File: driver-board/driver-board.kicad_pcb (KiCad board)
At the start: 2 copper layers, 22 parts, among them J1 MCP4725, J2 Conn_Coaxial, SW1 RST, U1 Pico, U2 MIC5317, U3 TSV358, U4 TSV358, U5 TCBT-2R5G

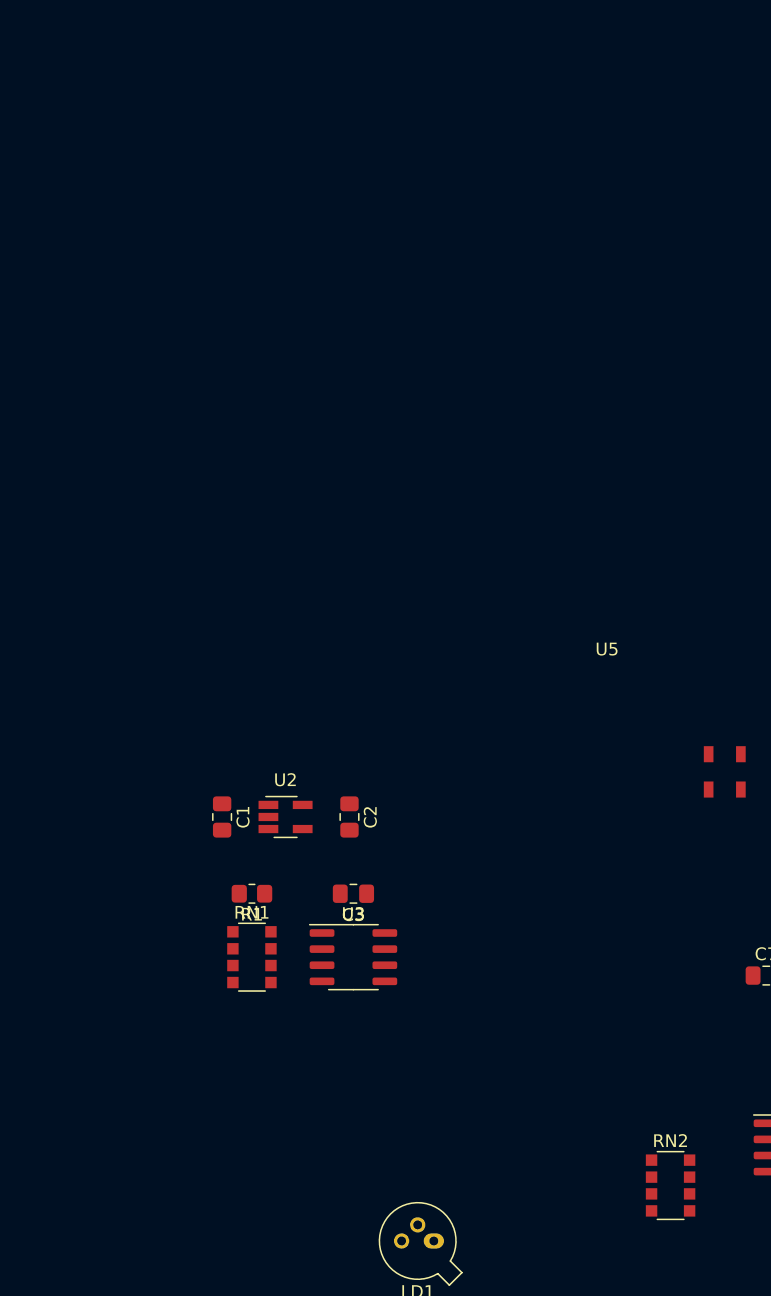
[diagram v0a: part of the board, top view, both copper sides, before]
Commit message: fix pot footprint
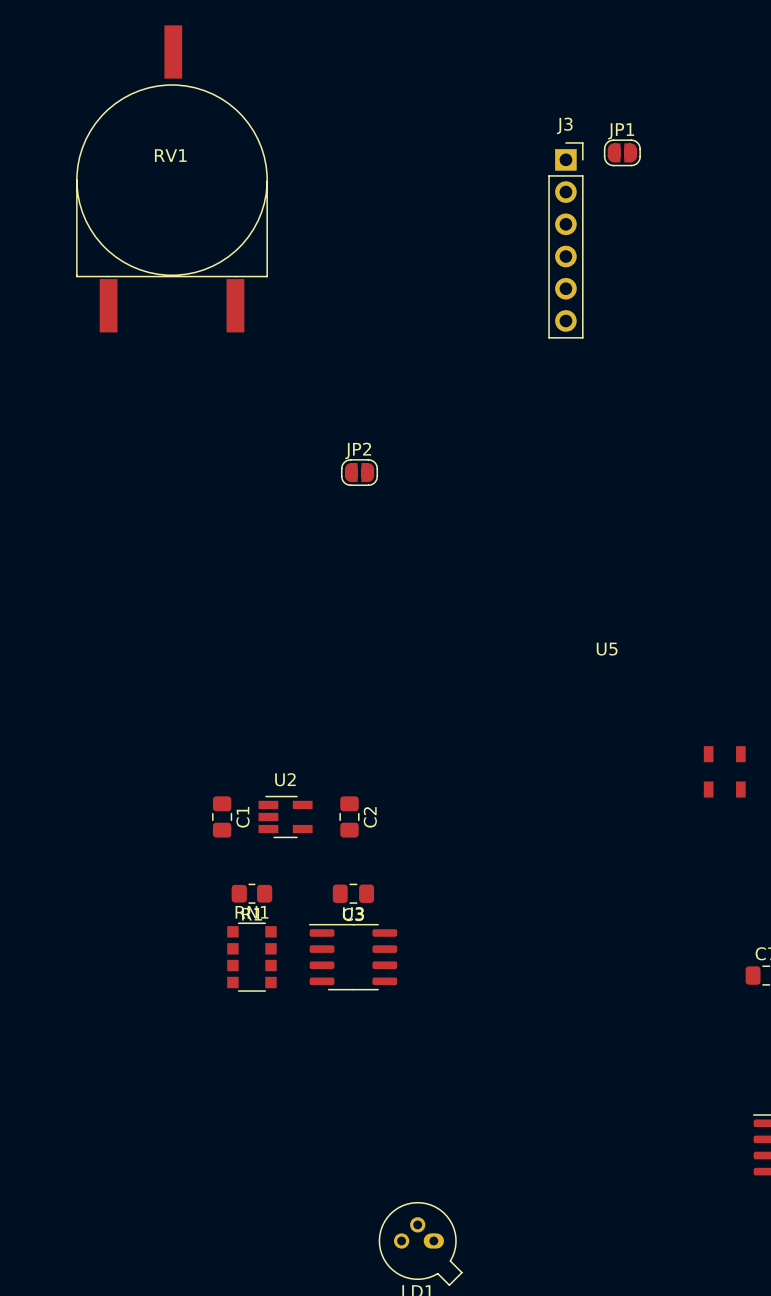
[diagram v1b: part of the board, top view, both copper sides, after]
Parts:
- removed RN2: R_Pack04_SIP_Split, Resistor_SMD:R_Array_Convex_4x1206
- added J3: MCP4725, Connector_PinSocket_2.54mm:PinSocket_1x06_P2.54mm_Vertical, F.Cu at (148.8, 59.1)
- added JP1: SolderJumper_2_Open, Jumper:SolderJumper-2_P1.3mm_Open_RoundedPad1.0x1.5mm, F.Cu at (153.2, 58.6)
- added JP2: SolderJumper_2_Open, Jumper:SolderJumper-2_P1.3mm_Open_RoundedPad1.0x1.5mm, F.Cu at (132.5, 83.8)
- added RV1: R_Potentiometer, lib:PT15-RV15, F.Cu at (117.7, 60.8)
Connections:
- net DAC_OUT renamed DAC_OUT_I_SRC
- U4 pad 5: Net-(U4-Pad1) -> Net-(U4-Pad5)

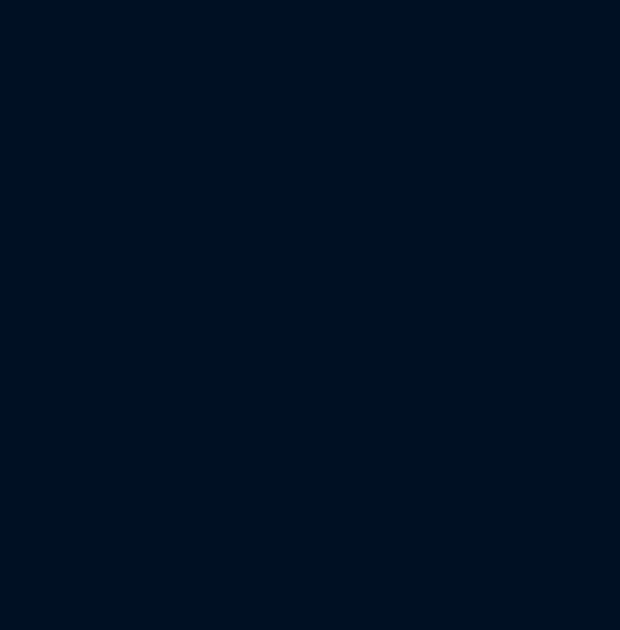
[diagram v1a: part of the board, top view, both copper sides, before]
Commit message: more test points and design rules
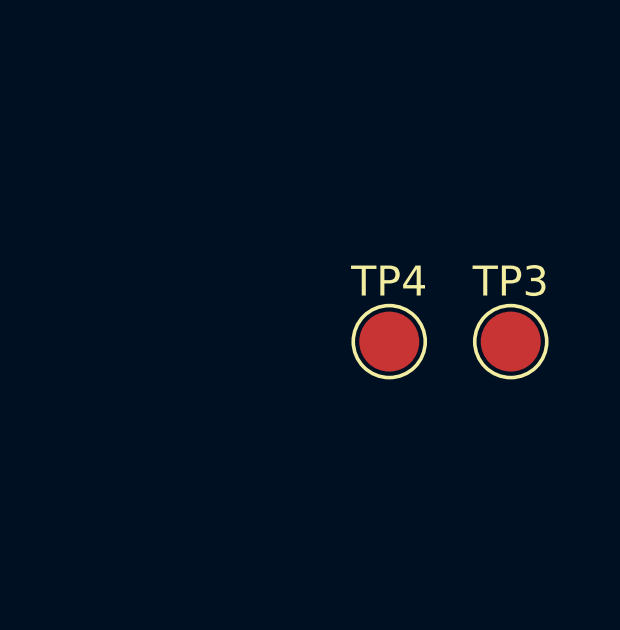
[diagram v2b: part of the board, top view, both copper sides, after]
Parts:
- added TP3: TestPoint, TestPoint:TestPoint_Pad_D2.0mm, F.Cu at (191.7, 71.3)
- added TP4: TestPoint, TestPoint:TestPoint_Pad_D2.0mm, F.Cu at (187.7, 71.3)
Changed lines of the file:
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@@
     (0 "F.Cu" signal)
     (31 "B.Cu" signal)
-    (32 "B.Adhes" user "B.Adhesive")
-    (33 "F.Adhes" user "F.Adhesive")
-    (34 "B.Paste" user)
-    (35 "F.Paste" user)
     (36 "B.SilkS" user "B.Silkscreen")
     (37 "F.SilkS" user "F.Silkscreen")
@@
     (40 "Dwgs.User" user "User.Drawings")
     (41 "Cmts.User" user "User.Comments")
-    (42 "Eco1.User" user "User.Eco1")
-    (43 "Eco2.User" user "User.Eco2")
     (44 "Edge.Cuts" user)
     (45 "Margin" user)
@@
     (48 "B.Fab" user)
     (49 "F.Fab" user)
-    (50 "User.1" user)
-    (51 "User.2" user)
-    (52 "User.3" user)
-    (53 "User.4" user)
-    (54 "User.5" user)
-    (55 "User.6" user)
-    (56 "User.7" user)
-    (57 "User.8" user)
-    (58 "User.9" user)
   )
   (setup
+    (stackup
+      (layer "F.SilkS" (type "Top Silk Screen"))
+      (layer "F.Mask" (type "Top Solder Mask") (thickness 0.01))
+      (layer "F.Cu" (type "copper") (thickness 0.035))
+      (layer "dielectric 1" (type "core") (thickness 1.51) (material "FR4") (epsilon_r 4.5) (loss_tangent 0.02))
+      (layer "B.Cu" (type "copper") (thickness 0.035))
+      (layer "B.Mask" (type "Bottom Solder Mask") (thickness 0.01))
+      (layer "B.SilkS" (type "Bottom Silk Screen"))
+      (copper_finish "None")
+      (dielectric_constraints no)
+    )
     (pad_to_mask_clearance 0)
     (pcbplotparams
@@
   (net 43 "unconnected-(U1-Pad42)")
   (net 44 "unconnected-(U1-Pad43)")
-  (net 45 "Net-(U4-Pad1)")
+  (net 45 "Net-(JP1-Pad1)")
   (net 46 "unconnected-(U5-Pad2)")
   (net 47 "DAC_OUT_TIA")
-  (net 48 "Net-(U4-Pad5)")
+  (net 48 "Net-(JP1-Pad2)")
   (net 49 "Net-(RN1-Pad3)")
   (net 50 "Net-(RN1-Pad5)")
-  (net 51 "Net-(U4-Pad3)")
+  (net 51 "Net-(RV1-Pad2)")
   (footprint "Capacitor_SMD:C_0805_2012Metric_Pad1.18x1.45mm_HandSolder" (layer "F.Cu")
     (at 174 128)
@@
       (net 36 "A3V3") (pinfunction "1") (pintype "passive"))
     (pad "2" smd rect (at 0.1 -10.1) (size 1.4 4.2) (layers "F.Cu" "F.Paste" "F.Mask")
-      (net 51 "Net-(U4-Pad3)") (pinfunction "2") (pintype "passive"))
+      (net 51 "Net-(RV1-Pad2)") (pinfunction "2") (pintype "passive"))
     (pad "3" smd rect (at 5 9.9) (size 1.4 4.2) (layers "F.Cu" "F.Paste" "F.Mask")
       (net 2 "GND") (pinfunction "3") (pintype "passive"))
+  )
+  (footprint "TestPoint:TestPoint_Pad_D2.0mm" (layer "F.Cu")
+    (at 187.65 71.3)
+    (descr "SMD pad as test Point, diameter 2.0mm")
+    (tags "test point SMD pad")
+    (property "Sheetfile" "driver-board.kicad_sch")
+    (property "Sheetname" "")
+    (attr exclude_from_pos_files)
+    (fp_text reference "TP4" (at 0 -1.998) (layer "F.SilkS")
+      (effects (font (size 1 1) (thickness 0.15)))
+    )
+    (fp_text value "TestPoint" (at 0 2.05) (layer "F.Fab")
+      (effects (font (size 1 1) (thickness 0.15)))
+    )
+    (fp_text user "${REFERENCE}" (at 0 -2) (layer "F.Fab")
+      (effects (font (size 1 1) (thickness 0.15)))
+    )
+    (fp_circle (center 0 0) (end 0 1.2) (layer "F.SilkS") (width 0.12) (fill none))
+    (fp_circle (center 0 0) (end 1.5 0) (layer "F.CrtYd") (width 0.05) (fill none))
+    (pad "1" smd circle locked (at 0 0) (size 2 2) (layers "F.Cu" "F.Mask")
+      (net 39 "TIA_OUT") (pinfunction "1") (pintype "passive"))
   )
   (footprint "Connector_PinSocket_2.54mm:PinSocket_1x06_P2.54mm_Vertical" (layer "F.Cu")
@@
     (fp_line (start -1.65 -1.25) (end 1.65 -1.25) (layer "F.CrtYd") (width 0.05))
     (pad "1" smd custom locked (at -0.65 0) (size 1 0.5) (layers "F.Cu" "F.Mask")
-      (net 45 "Net-(U4-Pad1)") (pinfunction "A") (pintype "passive") (zone_connect 2)
+      (net 45 "Net-(JP1-Pad1)") (pinfunction "A") (pintype "passive") (zone_connect 2)
       (options (clearance outline) (anchor rect))
       (primitives
@@
       ))
     (pad "2" smd custom locked (at 0.65 0) (size 1 0.5) (layers "F.Cu" "F.Mask")
-      (net 48 "Net-(U4-Pad5)") (pinfunction "B") (pintype "passive") (zone_connect 2)
+      (net 48 "Net-(JP1-Pad2)") (pinfunction "B") (pintype "passive") (zone_connect 2)
       (options (clearance outline) (anchor rect))
       (primitives
@@
     (fp_line (start 1.95 2.45) (end -1.95 2.45) (layer "F.Fab") (width 0.1))
     (pad "1" smd roundrect (at -2.475 -1.905) (size 1.95 0.6) (layers "F.Cu" "F.Paste" "F.Mask") (roundrect_rratio 0.25)
-      (net 45 "Net-(U4-Pad1)") (pintype "output"))
+      (net 45 "Net-(JP1-Pad1)") (pintype "output"))
     (pad "2" smd roundrect (at -2.475 -0.635) (size 1.95 0.6) (layers "F.Cu" "F.Paste" "F.Mask") (roundrect_rratio 0.25)
-      (net 45 "Net-(U4-Pad1)") (pinfunction "-") (pintype "input"))
+      (net 45 "Net-(JP1-Pad1)") (pinfunction "-") (pintype "input"))
     (pad "3" smd roundrect (at -2.475 0.635) (size 1.95 0.6) (layers "F.Cu" "F.Paste" "F.Mask") (roundrect_rratio 0.25)
-      (net 51 "Net-(U4-Pad3)") (pinfunction "+") (pintype "input"))
+      (net 51 "Net-(RV1-Pad2)") (pinfunction "+") (pintype "input"))
     (pad "4" smd roundrect (at -2.475 1.905) (size 1.95 0.6) (layers "F.Cu" "F.Paste" "F.Mask") (roundrect_rratio 0.25)
       (net 2 "GND") (pinfunction "V-") (pintype "power_in"))
     (pad "5" smd roundrect (at 2.475 1.905) (size 1.95 0.6) (layers "F.Cu" "F.Paste" "F.Mask") (roundrect_rratio 0.25)
-      (net 48 "Net-(U4-Pad5)") (pinfunction "+") (pintype "input"))
+      (net 48 "Net-(JP1-Pad2)") (pinfunction "+") (pintype "input"))
     (pad "6" smd roundrect (at 2.475 0.635) (size 1.95 0.6) (layers "F.Cu" "F.Paste" "F.Mask") (roundrect_rratio 0.25)
       (net 38 "PD") (pinfunction "-") (pintype "input"))
@@
       ))
     (pad "2" smd custom locked (at 0.65 0) (size 1 0.5) (layers "F.Cu" "F.Mask")
-      (net 48 "Net-(U4-Pad5)") (pinfunction "B") (pintype "passive") (zone_connect 2)
+      (net 48 "Net-(JP1-Pad2)") (pinfunction "B") (pintype "passive") (zone_connect 2)
       (options (clearance outline) (anchor rect))
       (primitives
@@
   )
   (footprint "TestPoint:TestPoint_Pad_D2.0mm" (layer "F.Cu")
+    (at 191.7 71.3)
+    (descr "SMD pad as test Point, diameter 2.0mm")
+    (tags "test point SMD pad")
+    (property "Sheetfile" "driver-board.kicad_sch")
+    (property "Sheetname" "")
+    (attr exclude_from_pos_files)
+    (fp_text reference "TP3" (at 0 -1.998) (layer "F.SilkS")
+      (effects (font (size 1 1) (thickness 0.15)))
+    )
+    (fp_text value "TestPoint" (at 0 2.05) (layer "F.Fab")
+      (effects (font (size 1 1) (thickness 0.15)))
+    )
+    (fp_text user "${REFERENCE}" (at 0 -2) (layer "F.Fab")
+      (effects (font (size 1 1) (thickness 0.15)))
+    )
+    (fp_circle (center 0 0) (end 0 1.2) (layer "F.SilkS") (width 0.12) (fill none))
+    (fp_circle (center 0 0) (end 1.5 0) (layer "F.CrtYd") (width 0.05) (fill none))
+    (pad "1" smd circle locked (at 0 0) (size 2 2) (layers "F.Cu" "F.Mask")
+      (net 48 "Net-(JP1-Pad2)") (pinfunction "1") (pintype "passive"))
+  )
+  (footprint "TestPoint:TestPoint_Pad_D2.0mm" (layer "F.Cu")

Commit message: temp
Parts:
- added C8: 0, Capacitor_SMD:C_0805_2012Metric_Pad1.18x1.45mm_HandSolder, F.Cu at (128.0, 84.3)
- added C9: 0, Capacitor_SMD:C_0805_2012Metric_Pad1.18x1.45mm_HandSolder, F.Cu at (131.5, 84.3)
- added J4: Conn_01x06_Male, Connector_PinHeader_2.54mm:PinHeader_1x06_P2.54mm_Vertical, F.Cu at (103.4, 97.8)
- added J5: Conn_01x06_Male, Connector_PinHeader_2.54mm:PinHeader_1x06_P2.54mm_Vertical, F.Cu at (108.6, 97.8)
- added JP3: SolderJumper_2_Open, Jumper:SolderJumper-2_P1.3mm_Open_RoundedPad1.0x1.5mm, F.Cu at (116.8, 114.8)
- C5, J1, J2, J3, LD1, SW1, U5: moved to B.Cu
- TP1, TP2, TP3, TP4: footprint TestPoint:TestPoint_Pad_D2.0mm -> TestPoint:TestPoint_Pad_D1.5mm
- moved J3 101.5 mm to (57.1, 102.7)
- moved J1 88.2 mm to (93.3, 110.3), turned to 180 degrees
- moved TP3 75.8 mm to (131.5, 117.5)
- moved RV1 70.8 mm to (126.2, 131.1), turned to 90 degrees
- moved TP4 66.9 mm to (131.3, 107.5)
- moved J2 66.9 mm to (157.1, 77.8)
- moved JP1 64.1 mm to (116.7, 111.3), turned to 180 degrees
- moved TP1 61.6 mm to (116.5, 102.3)
- moved LD1 57.8 mm to (165.9, 93.5), turned to -90 degrees
- moved TP2 53.1 mm to (128.5, 101.6)
- moved U4 49.3 mm to (124.5, 112.0)
- moved C4 48.3 mm to (125.8, 106.7)
- moved C5 44.2 mm to (151.4, 90.0), turned to -90 degrees
- moved R2 44.2 mm to (131.3, 111.7), turned to 90 degrees
- moved C6 36.6 mm to (138.3, 111.7), turned to 90 degrees
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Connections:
- J1 pad 3: SCL -> SCL0
- J1 pad 4: SDA -> SDA0
- J3 pad 3: SCL -> SCL1
- J3 pad 4: SDA -> SDA1
- U1 pad 26: SDA -> SDA0
- U1 pad 27: SCL -> SCL0
- U1 pad 35: A3V3 -> unconnected-(U1-Pad35)
- U1 pad 6: unconnected-(U1-Pad6) -> SDA1
- U1 pad 7: unconnected-(U1-Pad7) -> SCL1
- U4 pad 3: Net-(RV1-Pad2) -> Net-(U4-Pad3)
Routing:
- net DAC_OUT_TIA: track 0.00 -> 132.6 mm, vias 0 -> 2
- net TIA_OUT: track 0.00 -> 59.1 mm
- net A3V3: track 0.00 -> 53.0 mm
- net PD: track 0.00 -> 52.6 mm, vias 0 -> 1
- net 5V: track 0.00 -> 46.6 mm
- net DAC_OUT_I_SRC: track 0.00 -> 43.3 mm
- net Net-(C5-Pad2): track 0.00 -> 32.8 mm, vias 0 -> 1
- net Net-(JP1-Pad2): track 0.00 -> 22.4 mm, vias 0 -> 2
- net Net-(R1-Pad2): track 0.00 -> 19.4 mm, vias 0 -> 2
- net GND: track 0.00 -> 18.5 mm, vias 0 -> 84
- net Net-(U3-Pad6): track 0.00 -> 17.5 mm
- net Net-(RV1-Pad2): track 0.00 -> 16.2 mm, vias 0 -> 2
- net Net-(J2-Pad1): track 0.00 -> 12.8 mm
- net Net-(SW1-Pad1): track 0.00 -> 12.2 mm, vias 0 -> 1
- net SDA1: track 0.00 -> 10.00 mm
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- added copper zone on F.Cu, net 3V3
- added copper zone on F.Cu, net A3V3
- added copper zone on B.Cu, net GND
- added copper zone on F.Cu, net GND
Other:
- board outline added: 116.2 x 69.9 mm

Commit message: Anything
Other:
- board size 116.2 x 69.9 mm -> 157.7 x 69.9 mm
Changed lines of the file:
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@@
     (39 "F.Mask" user)
     (40 "Dwgs.User" user "User.Drawings")
-    (41 "Cmts.User" user "User.Comments")
     (44 "Edge.Cuts" user)
     (45 "Margin" user)
     (46 "B.CrtYd" user "B.Courtyard")
     (47 "F.CrtYd" user "F.Courtyard")
-    (48 "B.Fab" user)
-    (49 "F.Fab" user)
   )
   (setup
@@
   )
   (gr_line (start 53.75 134.5) (end 53.75 74.5) (layer "Edge.Cuts") (width 0.15))
+  (gr_arc (start 208 129.8) (mid 209.649643 128.047236) (end 211.302498 129.8) (layer "Edge.Cuts") (width 0.1))
   (gr_line (start 169.75 74.5) (end 169.75 144.45) (layer "Edge.Cuts") (width 0.15))
   (gr_line (start 169.75 144.45) (end 53.6 144.45) (layer "Edge.Cuts") (width 0.15))

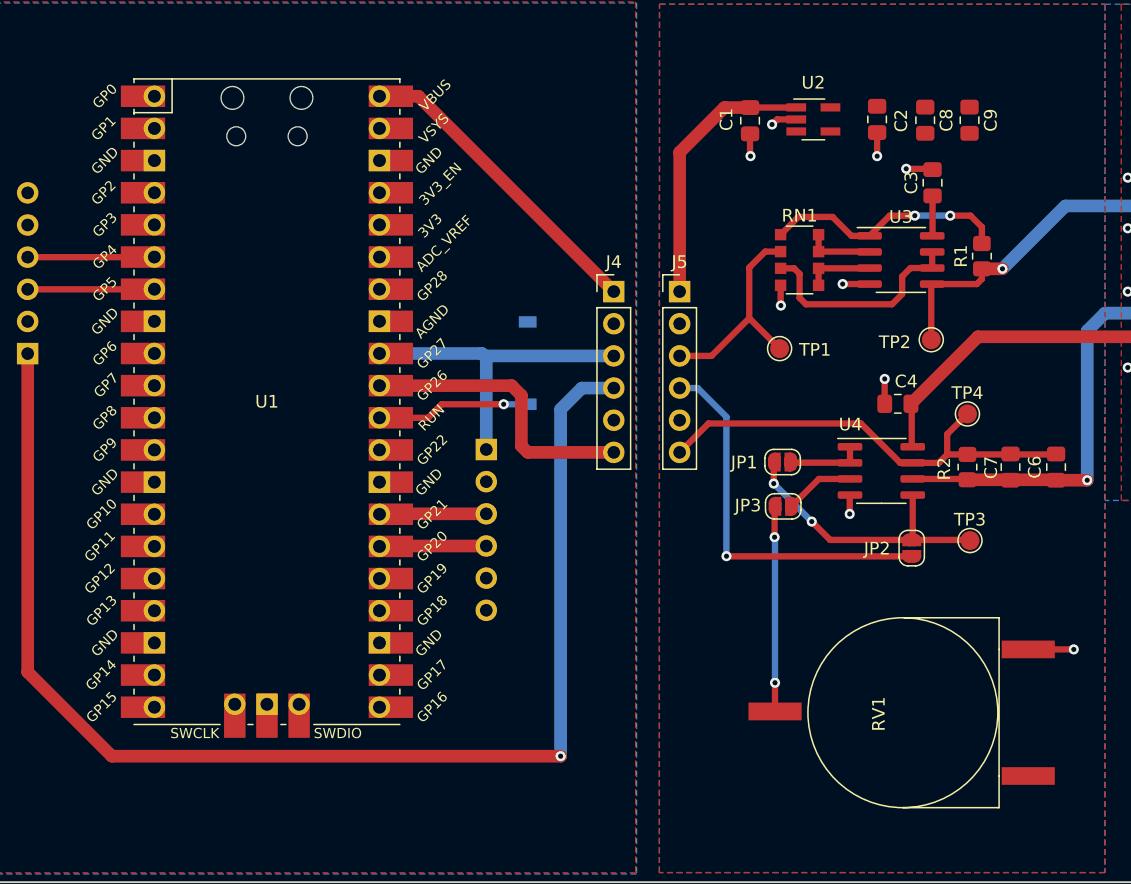
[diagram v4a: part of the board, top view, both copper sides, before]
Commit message: pico modified sym/fp
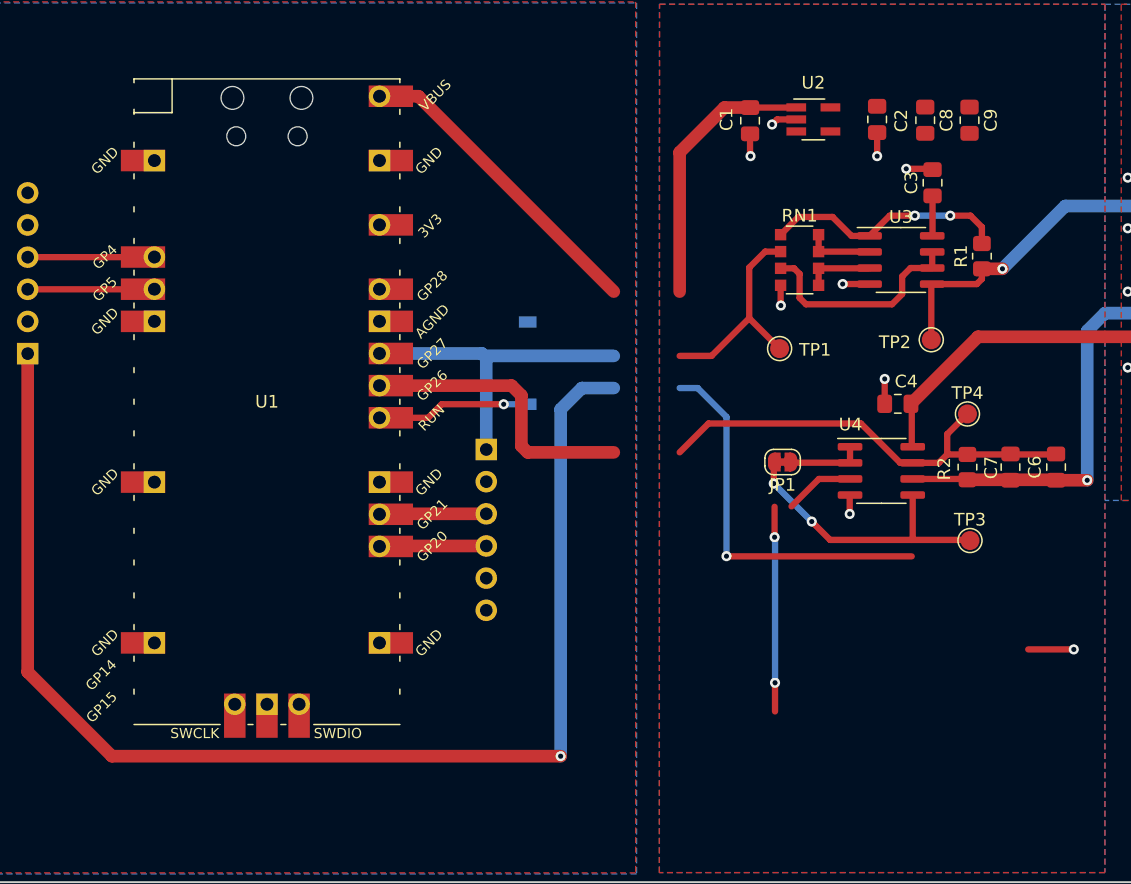
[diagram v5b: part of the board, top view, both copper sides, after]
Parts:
- removed J4, J5: Conn_01x06_Male, Connector_PinHeader_2.54mm:PinHeader_1x06_P2.54mm_Vertical
- removed JP2, JP3: SolderJumper_2_Open, Jumper:SolderJumper-2_P1.3mm_Open_RoundedPad1.0x1.5mm
- removed RV1: R_Potentiometer, lib:PT15-RV15
- JP1: footprint Jumper:SolderJumper-2_P1.3mm_Open_RoundedPad1.0x1.5mm -> Jumper:SolderJumper-2_P1.3mm_Bridged_RoundedPad1.0x1.5mm
- U1: footprint lib:RPi_Pico_SMD_TH -> lib:RPi_Pico_minimal
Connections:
- JP1 pad 1: Net-(JP1-Pad1) -> DAC_OUT_TIA
- U4 pad 1: Net-(JP1-Pad1) -> (no net)
- U4 pad 2: Net-(JP1-Pad1) -> (no net)
- U4 pad 3: Net-(U4-Pad3) -> (no net)
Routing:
- net (no net): track 0.00 -> 21.7 mm, vias 0 -> 2
- net Net-(RV1-Pad2): track 16.2 -> 0.00 mm, vias 2 -> 0
- net Net-(JP1-Pad1): track 5.98 -> 0.00 mm
- net DAC_OUT_TIA: track 132.6 -> 138.6 mm
- net Net-(U4-Pad3): track 5.52 -> 0.00 mm
